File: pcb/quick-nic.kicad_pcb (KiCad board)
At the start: 6 copper layers, 50 x 20 mm, 25 parts, among them J1 HC-USB3.0-C26, U1 CH217A, U2 RTL8153B-VB-CG, Y1 25Mhz

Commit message: added mounting hole, might add honourable mentions next time before i send it off to fab
Signed-off-by: Toby Cm <toby@vsus.app>
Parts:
- added H1: MountingHole, MountingHole:MountingHole_3.2mm_M3_Pad, F.Cu at (142.0, 67.0)
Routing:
- net +5V: track 12.4 -> 17.3 mm, vias 7 -> 9
- net /LED0: track 37.0 -> 35.8 mm
- net /LED1: track 38.8 -> 37.6 mm
- net +3V3: track 17.8 -> 18.8 mm
- net /MDI3-: track 13.4 -> 12.8 mm
- net Net-(R2-Pad1): track 24.2 -> 23.7 mm

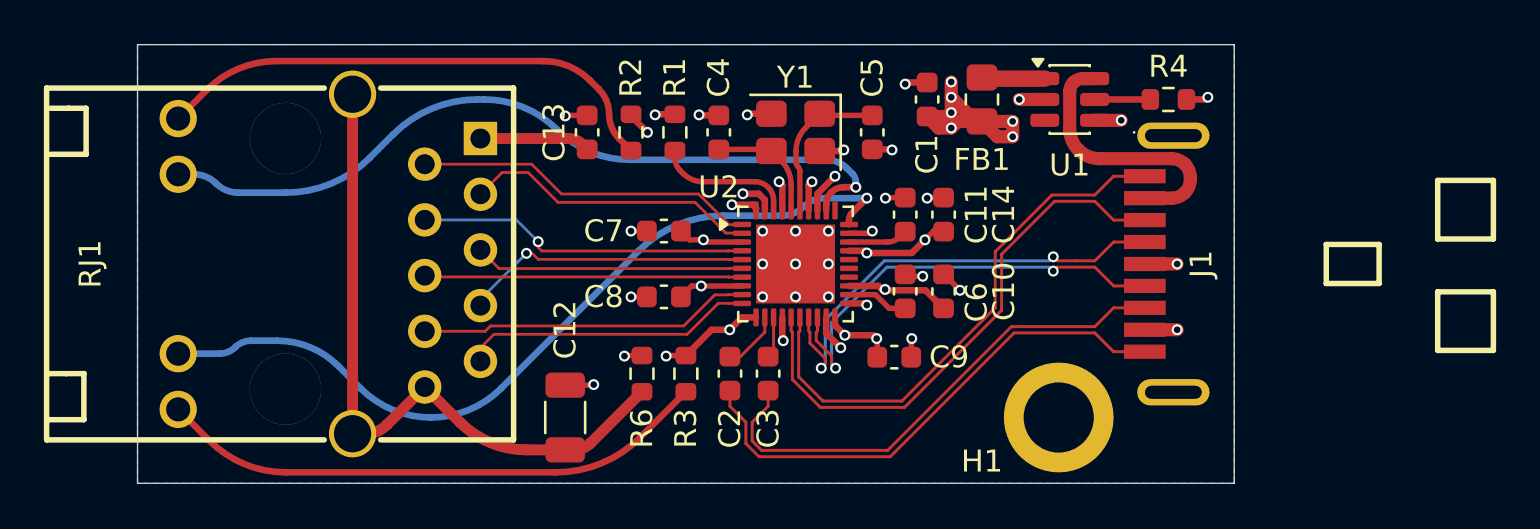
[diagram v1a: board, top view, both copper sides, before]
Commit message: length matched intra-pair diff pairs
Signed-off-by: Toby Cm <toby@vsus.app>
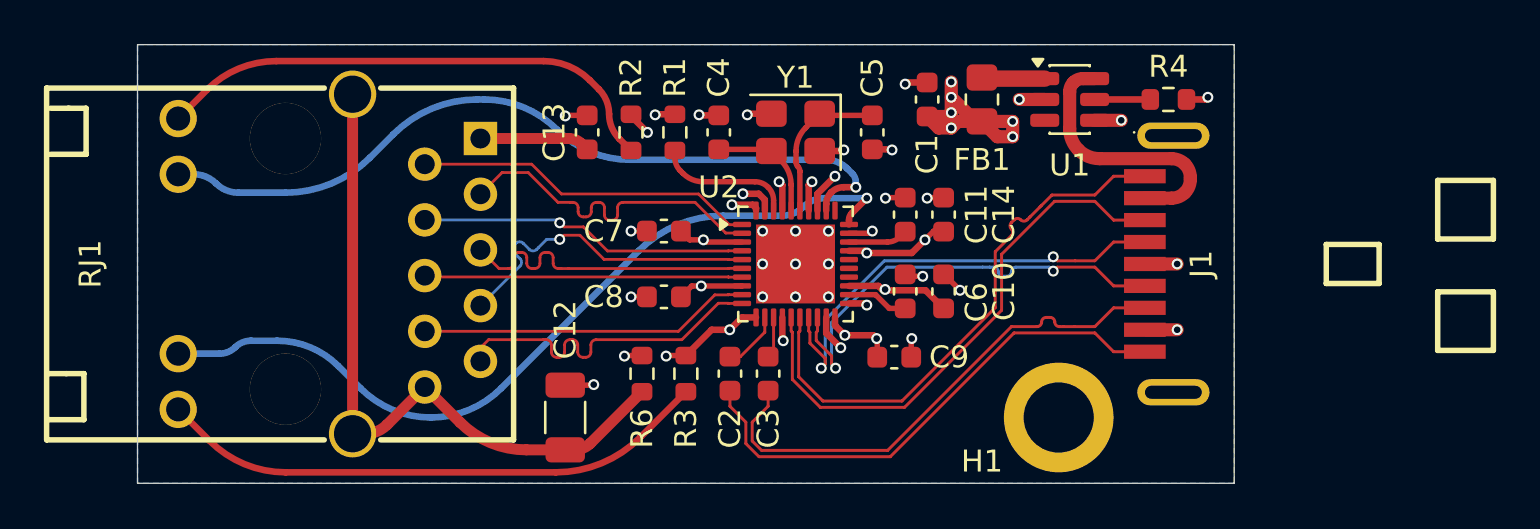
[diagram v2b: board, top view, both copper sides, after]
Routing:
- net /MDI3-: track 12.8 -> 15.1 mm
- net /MDI1-: track 12.9 -> 15.0 mm
- net /MDI0-: track 13.2 -> 15.2 mm
- net /MDI2+: track 12.3 -> 14.3 mm

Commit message: update pcb, add render, update readme, add fab packages, add ibom
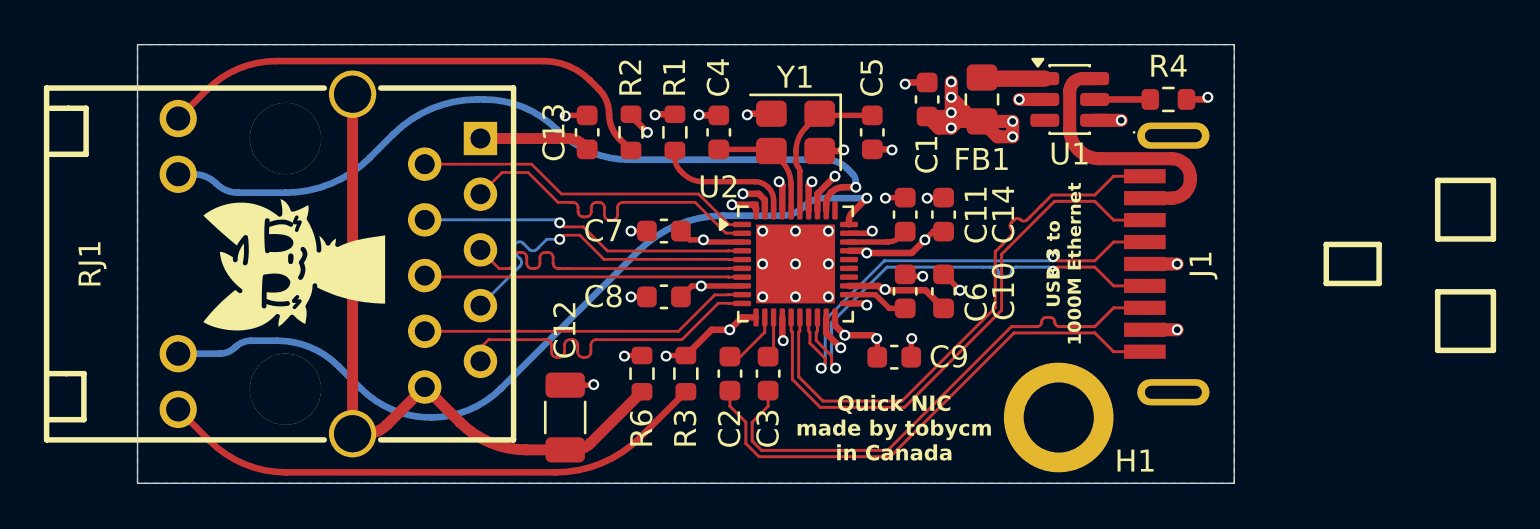
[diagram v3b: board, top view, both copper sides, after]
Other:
- board text added: "Honourable mentions: Pen High Hack Club"
- board text added: "Kate swn cloudglides duy Tanishq deltea yousef parking_turkeys in loving memories: i10 Tyson"
- board text added: "Madhav btz Arca KaiPereira Rudy julia do sofia froppii"
- board text added: "NoxAevi sanadaghat cubit010 dodge1 Simon Vejas"
- board text added: "Quick NIC made by tobycm in Canada"
- board text added: "USB 3 to 1000M Ethernet"
- board text added: "https://github.com/tobycm/quick-nic"
- board text added: "shn"
- board text added: "Արեգ"
